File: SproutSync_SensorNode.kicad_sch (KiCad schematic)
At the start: 0 parts

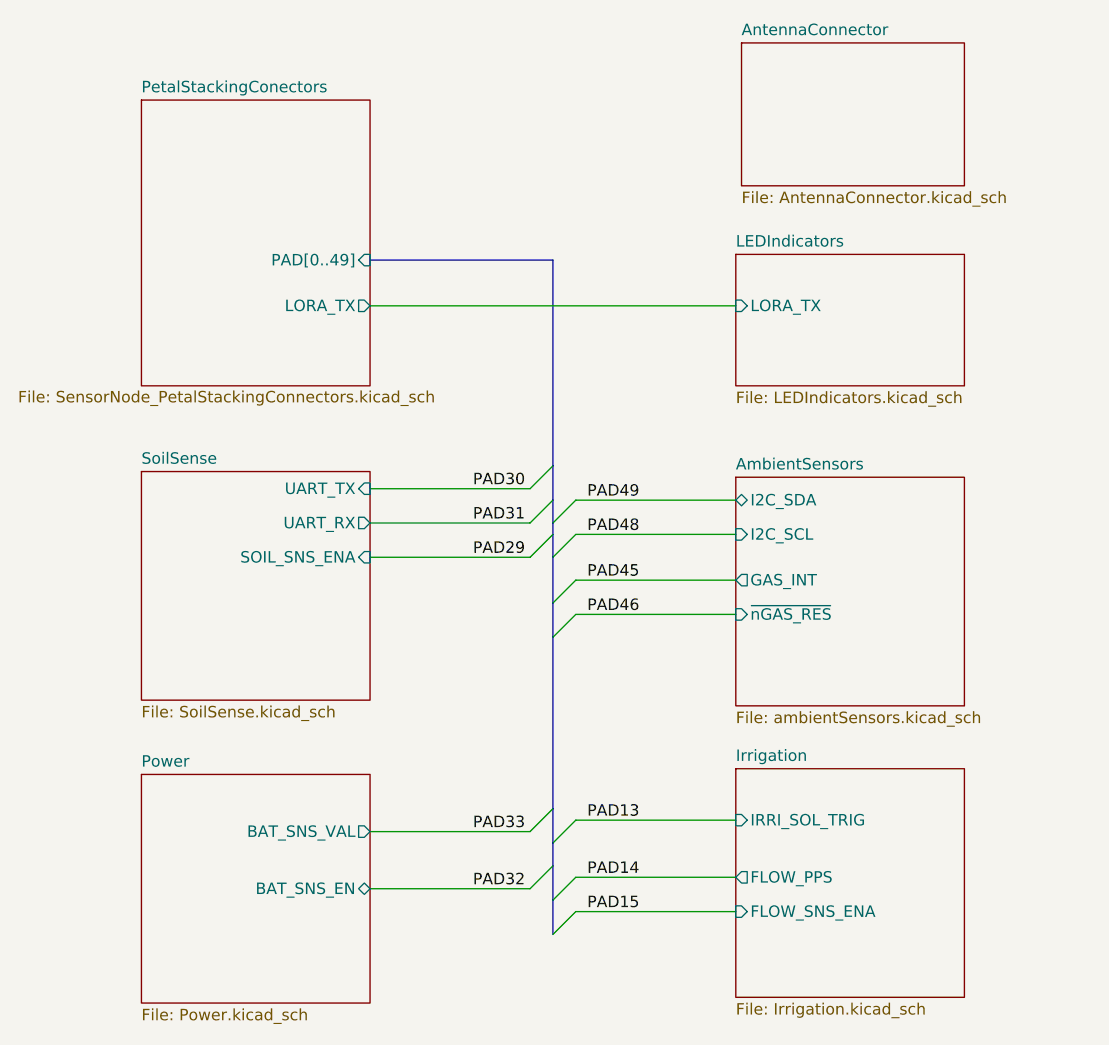
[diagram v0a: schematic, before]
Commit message: mostly routed
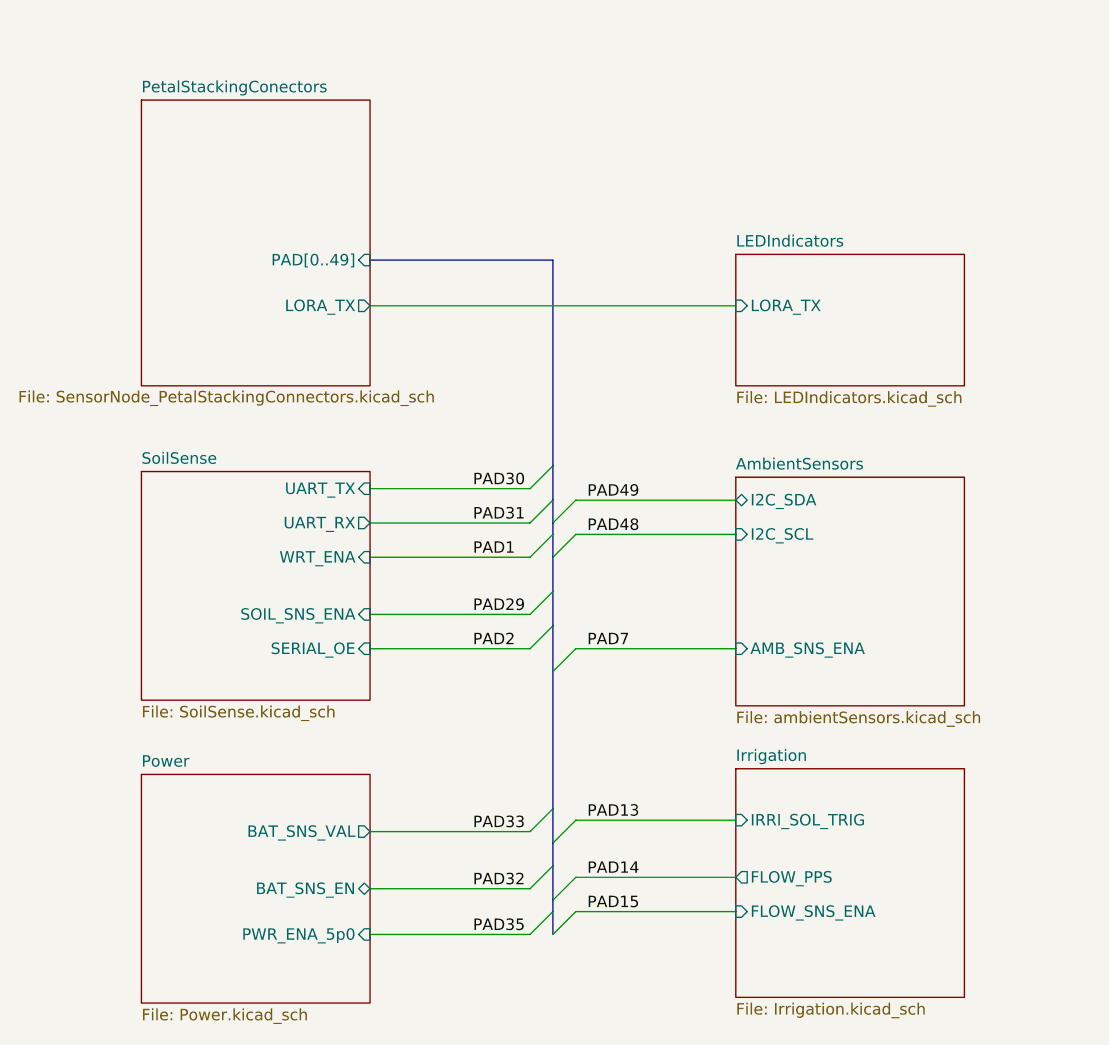
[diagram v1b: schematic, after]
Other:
- removed sheet AntennaConnector
- sheet AmbientSensors ports: added AMB_SNS_ENA; removed GAS_INT, ~{nGAS_RES}
- sheet Power ports: added PWR_ENA_5p0; removed none
- sheet SoilSense ports: added SERIAL_OE, WRT_ENA; removed none

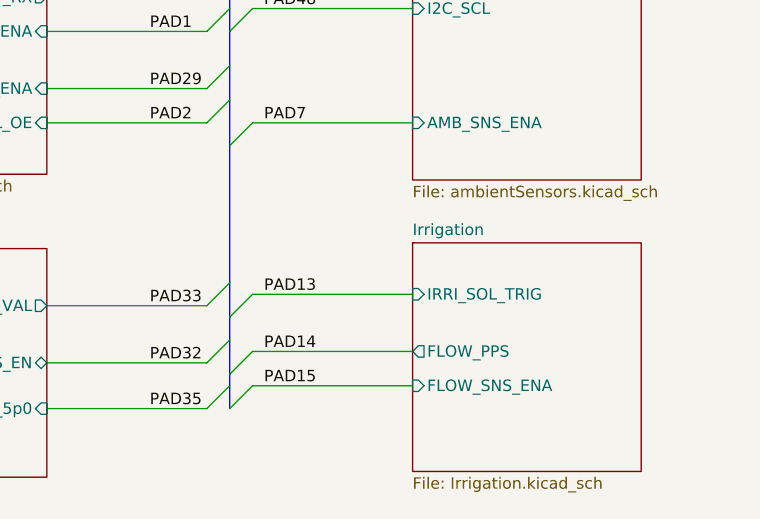
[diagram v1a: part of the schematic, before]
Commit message: Removed via in pads
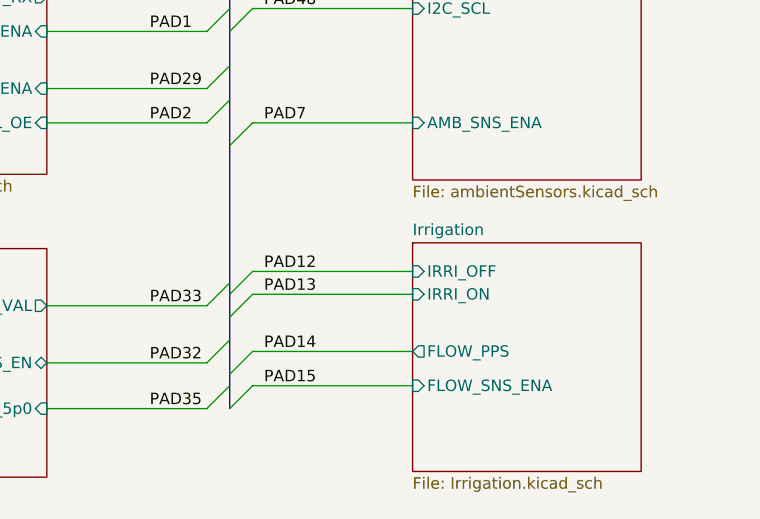
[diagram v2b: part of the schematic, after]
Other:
- sheet Irrigation ports: added IRRI_OFF, IRRI_ON; removed IRRI_SOL_TRIG
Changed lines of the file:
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@@
 		)
 	)
-	(bus
-		(pts
-			(xy 130.81 113.03) (xy 130.81 116.84)
+	(bus_entry
+		(at 130.81 114.3)
+		(size 2.54 -2.54)
+		(stroke
+			(width 0)
+			(type default)
+		)
+	)
+	(bus
+		(pts
+			(xy 130.81 113.03) (xy 130.81 114.3)
 		)
 		(stroke
@@
 	(bus
 		(pts
+			(xy 130.81 114.3) (xy 130.81 116.84)
+		)
+		(stroke
+			(width 0)
+			(type default)
+		)
+	)
+	(bus
+		(pts
 			(xy 130.81 88.9) (xy 130.81 92.71)
 		)
@@
 		(pts
 			(xy 133.35 120.65) (xy 151.13 120.65)
+		)
+		(stroke
+			(width 0)
+			(type default)
+		)
+	)
+	(wire
+		(pts
+			(xy 133.35 111.76) (xy 151.13 111.76)
 		)
 		(stroke
@@
 	(label "PAD13"
 		(at 134.62 114.3 0)
+		(effects
+			(font
+				(size 1.27 1.27)
+			)
+			(justify left bottom)
+		)
+	)
+	(label "PAD12"
+		(at 134.62 111.76 0)
 		(effects
 			(font
@@
 			)
 		)
-		(pin "IRRI_SOL_TRIG" input
-			(at 151.13 114.3 180)
-			(effects
-				(font
-					(size 1.27 1.27)
-				)
-				(justify left)
-			)
-		)
 		(pin "FLOW_PPS" output
 			(at 151.13 120.65 180)
@@
 			(effects
 				(font
+					(size 1.27 1.27)
+				)
+				(justify left)
+			)
+		)
+		(pin "IRRI_OFF" input
+			(at 151.13 111.76 180)
+			(effects
+				(font
+					(size 1.27 1.27)
+				)
+				(justify left)
+			)
+		)
+		(pin "IRRI_ON" input
+			(at 151.13 114.3 180)
+			(effects
+				(font

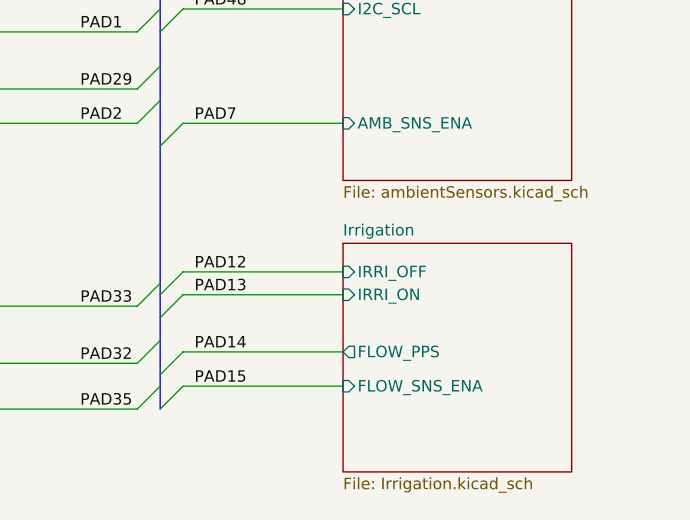
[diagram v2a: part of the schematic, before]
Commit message: Swapped H bridge and irrigation conn
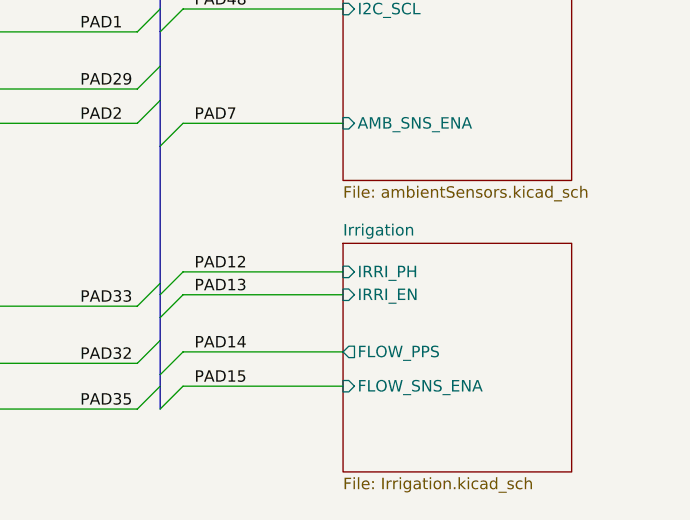
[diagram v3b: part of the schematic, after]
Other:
- sheet Irrigation ports: added IRRI_EN, IRRI_PH; removed IRRI_OFF, IRRI_ON
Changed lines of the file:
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@@
 			)
 		)
-		(pin "IRRI_OFF" input
-			(at 151.13 111.76 180)
+		(pin "IRRI_EN" input
+			(at 151.13 114.3 180)
 			(effects
 				(font
@@
 			)
 		)
-		(pin "IRRI_ON" input
-			(at 151.13 114.3 180)
+		(pin "IRRI_PH" input
+			(at 151.13 111.76 180)
 			(effects
 				(font
